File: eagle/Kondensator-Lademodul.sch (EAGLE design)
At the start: 26 parts, among them IC3 7818TV, X1 MKDSN1,5/2-5,08, X2 MKDSN1,5/2-5,08, X3 MKDSN1,5/2-5,08

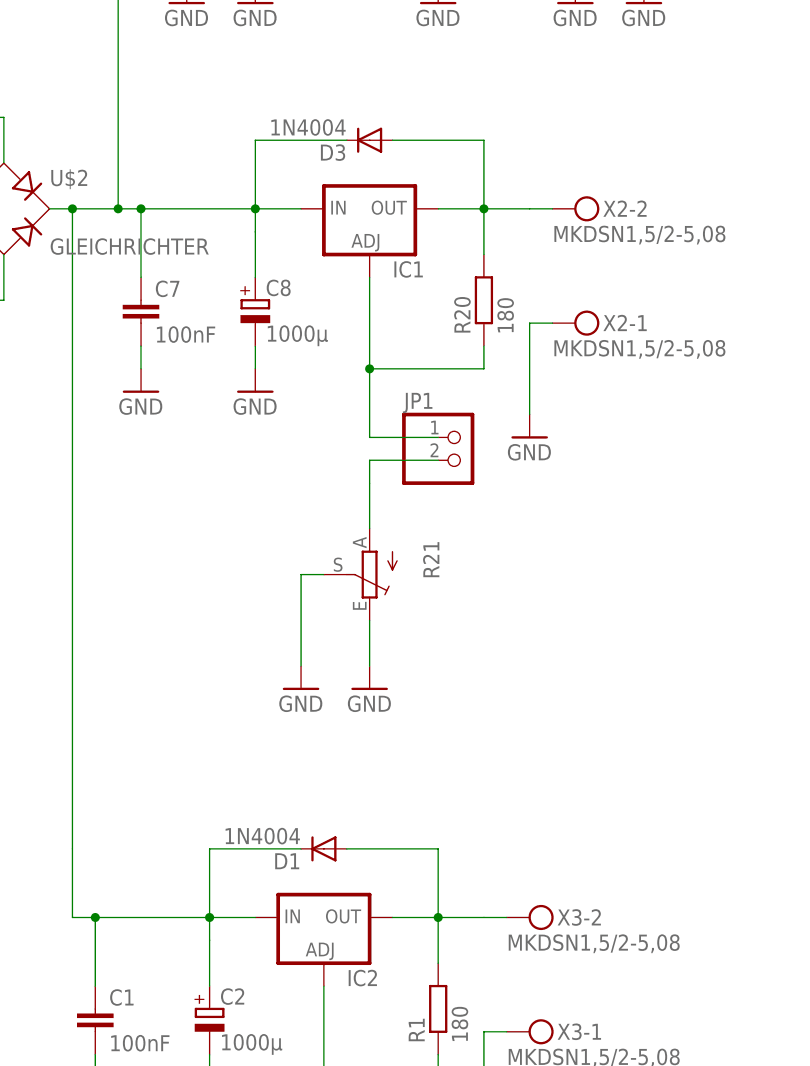
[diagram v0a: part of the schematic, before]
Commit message: Minor documentation changes, reduced size of vsens Resistor to detect contact
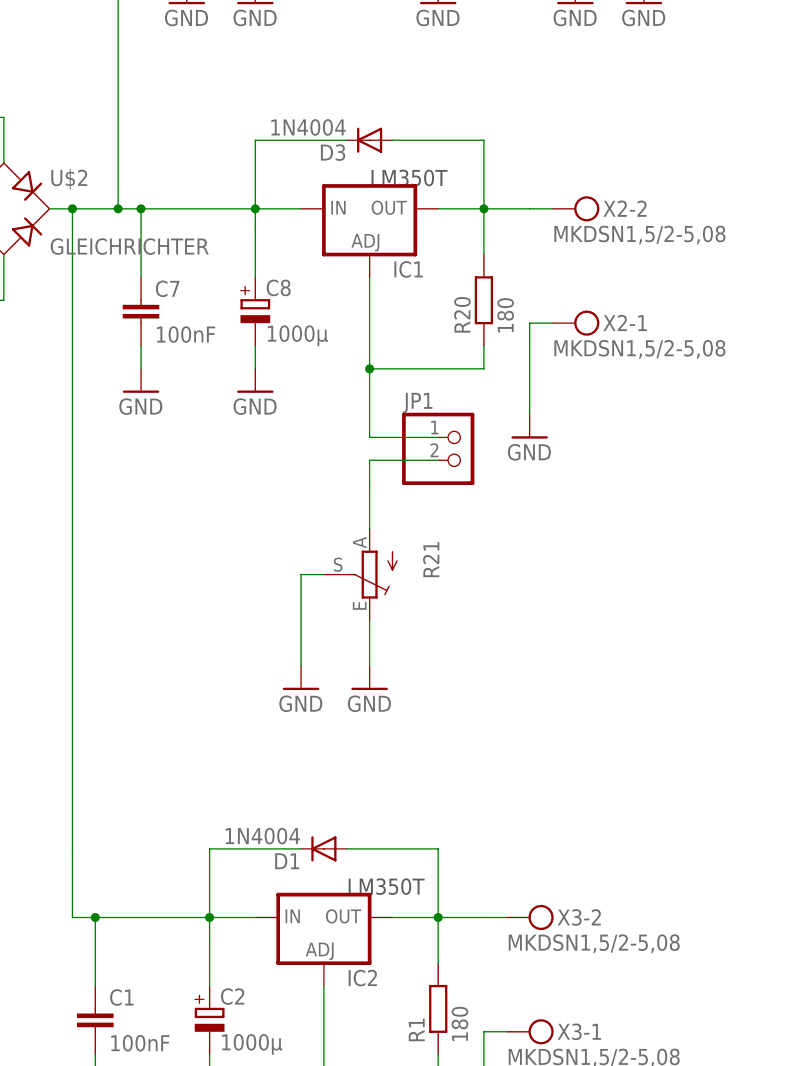
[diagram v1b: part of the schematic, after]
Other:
- note added: "LM350T"
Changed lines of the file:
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@@
 <sheet>
 <plain>
+<text x="-12.7" y="33.02" size="1.778" layer="97">LM350T</text>
+<text x="-15.24" y="-45.72" size="1.778" layer="97">LM350T</text>
 </plain>
 <instances>
